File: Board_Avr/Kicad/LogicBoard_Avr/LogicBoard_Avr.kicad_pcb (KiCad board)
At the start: 4 copper layers, 65 x 62 mm, 64 parts, among them J1 I2C_Interface, J10 PSU Connector, J11 TriggeredStatusLedConnector, J12 PowerStatusLedConnector, J2 UART_Interface, J3 Mechanical user interface mai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, J4 Power board connector, J5 SPI Connector, J6 ICSP Header, J9 GPIO Connector, SW1 Reset switch, U1 ATmega328PB-A, U2 TLP291, U3 NCP603SN330T1G, U4 LM1117-5.0, X1 ASV-12.000MHZ-EJ-T, Y1 ABLS-20.000MHz-16-A-4-H-T

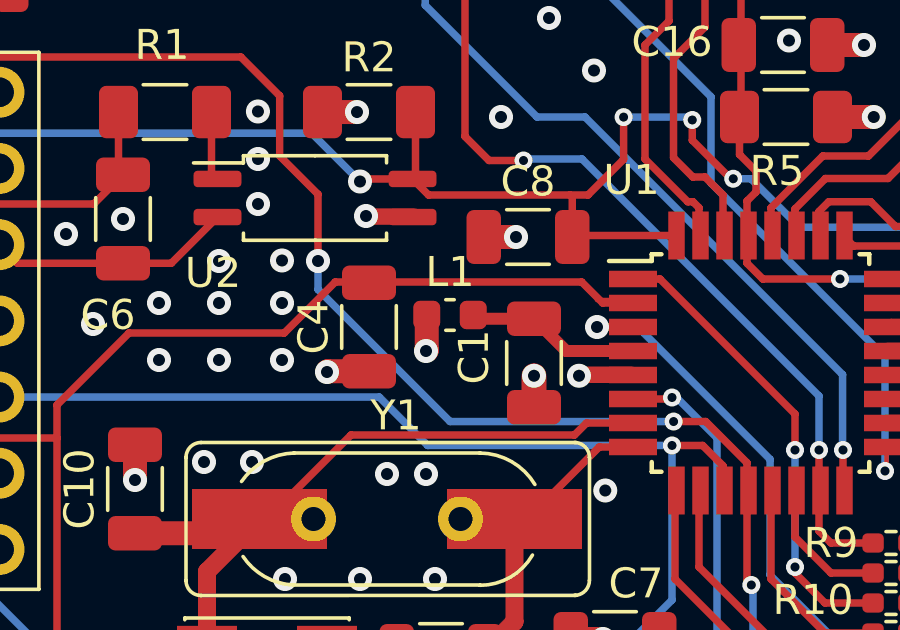
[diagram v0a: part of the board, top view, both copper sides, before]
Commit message: Updated ferrite bead footprint
Signed-off-by: bebenlebricolo <benoittarrade@hotmail.fr>
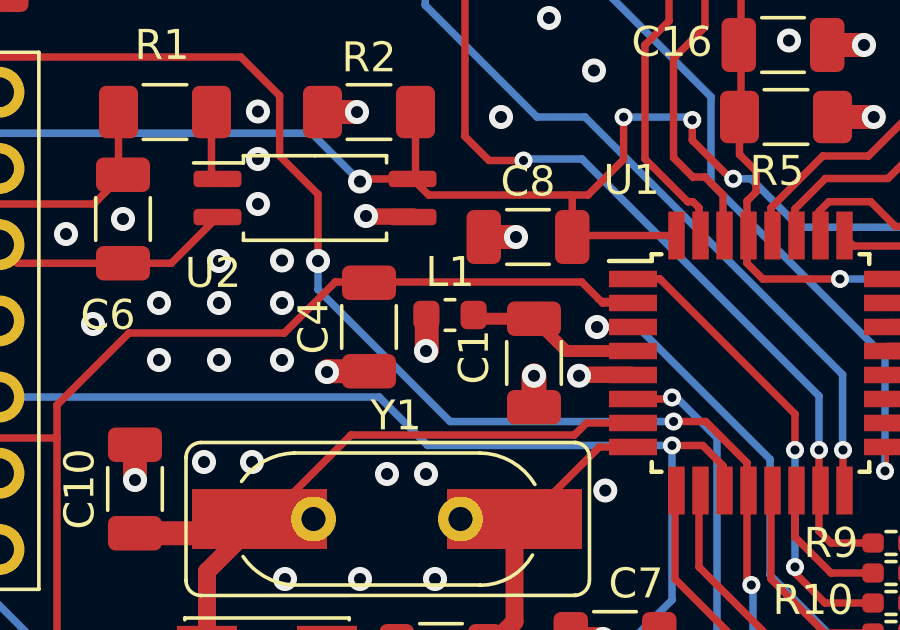
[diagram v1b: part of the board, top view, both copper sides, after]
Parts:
- L1: footprint Capacitor_SMD:C_0603_1608Metric -> Inductor_SMD:L_0603_1608Metric
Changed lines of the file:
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@@
     )
   )
-  (footprint "Capacitor_SMD:C_0603_1608Metric" (layer "F.Cu")
+  (footprint "Inductor_SMD:L_0603_1608Metric" (layer "F.Cu")
     (at 139.7 88.4)
-    (descr "Capacitor SMD 0603 (1608 Metric), square (rectangular) end terminal, IPC_7351 nominal, (Body size source: IPC-SM-782 page 76, https://www.pcb-3d.com/wordpress/wp-content/uploads/ipc-sm-782a_amendment_1_and_2.pdf), generated with kicad-footprint-generator")
-    (tags "capacitor")
+    (descr "Inductor SMD 0603 (1608 Metric), square (rectangular) end terminal, IPC_7351 nominal, (Body size source: http://www.tortai-tech.com/upload/download/2011102023233369053.pdf), generated with kicad-footprint-generator")
+    (tags "inductor")
     (property "Sheetfile" "LogicBoard_Avr.kicad_sch")
     (property "Sheetname" "")
@@
       (effects (font (size 0.4 0.4) (thickness 0.06)))
     )
-    (fp_line (start -0.14058 0.51) (end 0.14058 0.51) (layer "F.SilkS") (width 0.12))
-    (fp_line (start -0.14058 -0.51) (end 0.14058 -0.51) (layer "F.SilkS") (width 0.12))
-    (fp_line (start -1.48 0.73) (end -1.48 -0.73) (layer "F.CrtYd") (width 0.05))
-    (fp_line (start -1.48 -0.73) (end 1.48 -0.73) (layer "F.CrtYd") (width 0.05))
+    (fp_line (start -0.162779 -0.51) (end 0.162779 -0.51) (layer "F.SilkS") (width 0.12))
+    (fp_line (start -0.162779 0.51) (end 0.162779 0.51) (layer "F.SilkS") (width 0.12))
     (fp_line (start 1.48 -0.73) (end 1.48 0.73) (layer "F.CrtYd") (width 0.05))
     (fp_line (start 1.48 0.73) (end -1.48 0.73) (layer "F.CrtYd") (width 0.05))
+    (fp_line (start -1.48 -0.73) (end 1.48 -0.73) (layer "F.CrtYd") (width 0.05))
+    (fp_line (start -1.48 0.73) (end -1.48 -0.73) (layer "F.CrtYd") (width 0.05))
+    (fp_line (start -0.8 0.4) (end -0.8 -0.4) (layer "F.Fab") (width 0.1))
     (fp_line (start -0.8 -0.4) (end 0.8 -0.4) (layer "F.Fab") (width 0.1))
+    (fp_line (start 0.8 0.4) (end -0.8 0.4) (layer "F.Fab") (width 0.1))
     (fp_line (start 0.8 -0.4) (end 0.8 0.4) (layer "F.Fab") (width 0.1))
-    (fp_line (start -0.8 0.4) (end -0.8 -0.4) (layer "F.Fab") (width 0.1))
-    (fp_line (start 0.8 0.4) (end -0.8 0.4) (layer "F.Fab") (width 0.1))
-    (pad "1" smd roundrect locked (at -0.775 0) (size 0.9 0.95) (layers "F.Cu" "F.Paste" "F.Mask") (roundrect_rratio 0.25)
+    (pad "1" smd roundrect (at -0.7875 0) (size 0.875 0.95) (layers "F.Cu" "F.Paste" "F.Mask") (roundrect_rratio 0.25)
       (net 8 "/VCC") (pinfunction "1") (pintype "passive"))
-    (pad "2" smd roundrect locked (at 0.775 0) (size 0.9 0.95) (layers "F.Cu" "F.Paste" "F.Mask") (roundrect_rratio 0.25)
+    (pad "2" smd roundrect (at 0.7875 0) (size 0.875 0.95) (layers "F.Cu" "F.Paste" "F.Mask") (roundrect_rratio 0.25)
       (net 1 "/MCU_VCC") (pinfunction "2") (pintype "passive"))
-    (model "${KICAD6_3DMODEL_DIR}/Capacitor_SMD.3dshapes/C_0603_1608Metric.wrl"
+    (model "${KICAD6_3DMODEL_DIR}/Inductor_SMD.3dshapes/L_0603_1608Metric.wrl"
       (offset (xyz 0 0 0))
       (scale (xyz 1 1 1))

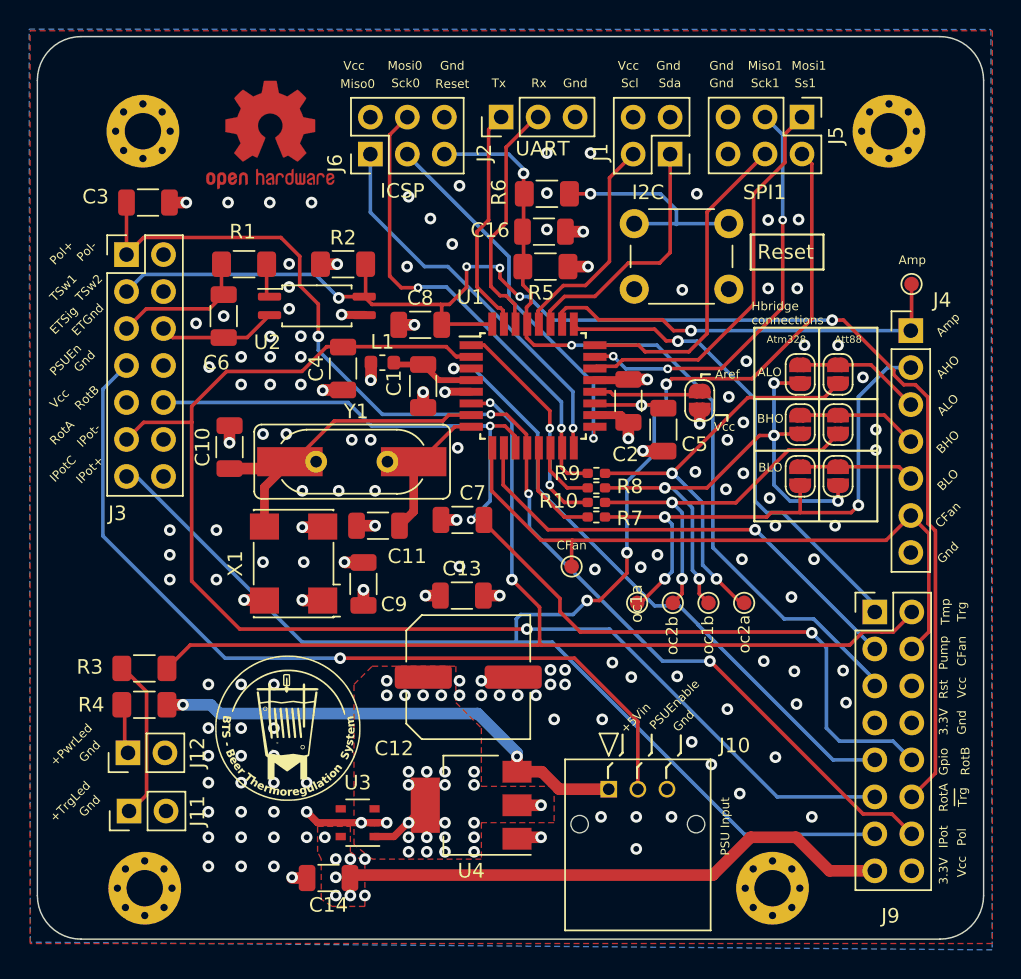
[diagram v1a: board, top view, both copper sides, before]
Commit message: Updated board with external clock for both mcus + thermal reliefs update
Signed-off-by: bebenlebricolo <benoittarrade@hotmail.fr>
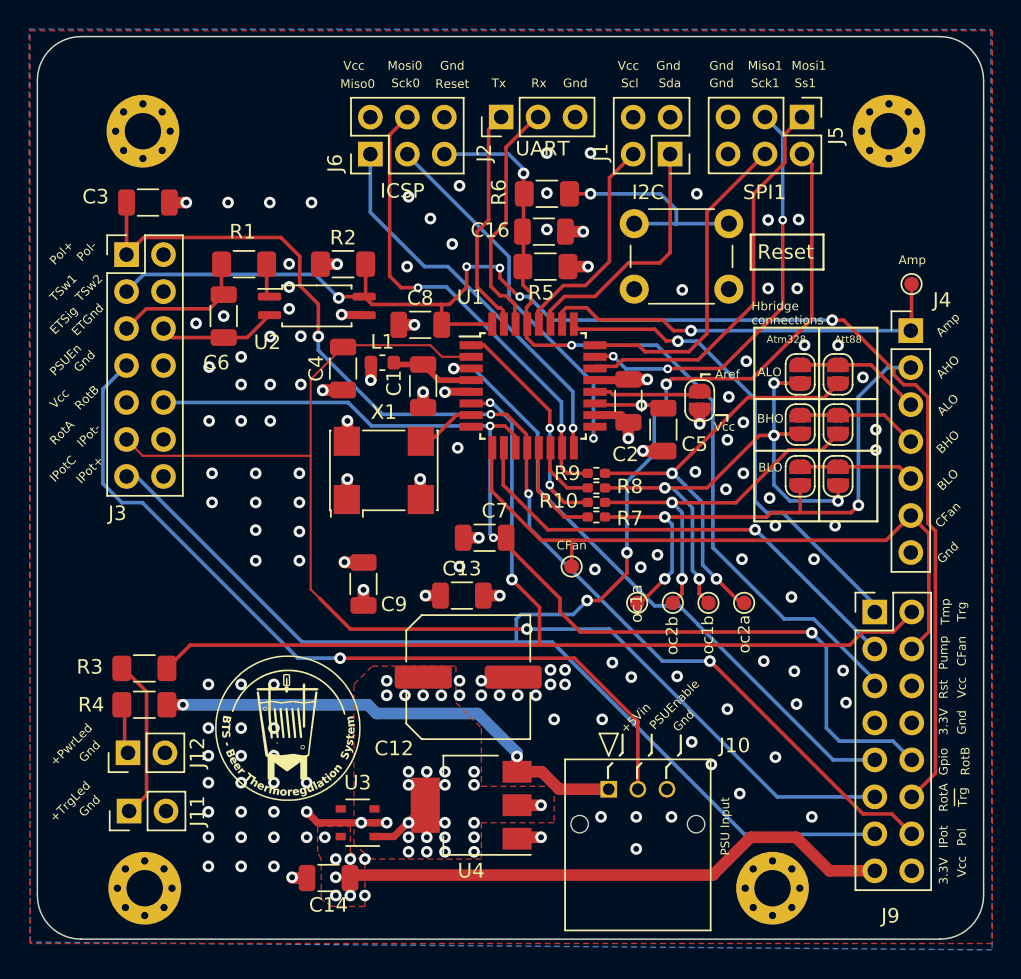
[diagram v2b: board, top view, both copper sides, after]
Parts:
- removed C10, C11: 10pF, Capacitor_SMD:C_1206_3216Metric
- removed REF**: OSHW-Logo2_9.8x8mm_Copper, Symbol:OSHW-Logo2_9.8x8mm_Copper
- removed REF**: OSHW-Logo2_14.6x12mm_SilkScreen, Symbol:OSHW-Logo2_14.6x12mm_SilkScreen
- removed Y1: ABLS-20.000MHz-16-A-4-H-T, BTS-LogicBoard:Crystal_SMD_TH_Combo_HC49-SD
- moved X1 8.91 mm to (139.8, 95.8), turned to 0 degrees
- moved C7 1.96 mm to (146.7, 100.4)
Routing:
- net /XTAL1: track 23.0 -> 4.21 mm
- net /XTAL2: track 9.70 -> 0.00 mm
- net /RotEncA(In): track 92.4 -> 84.5 mm
- net GND: track 30.3 -> 27.8 mm, vias 141 -> 136
- net /PSU_Enabled: track 59.1 -> 57.0 mm
- net /RotEncB(In): track 73.9 -> 72.3 mm
